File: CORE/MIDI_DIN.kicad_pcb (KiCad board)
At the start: 2 copper layers, 29.5 x 99.8 mm, 60 parts, among them J1 Conn_02x08_Odd_Even, J2 USB_C_Receptacle_USB2.0, J3 Conn_01x04, J5 MAB5100S, J6 MAB5100S, J7 Conn_01x06, Q1 MMBT3906, SW1 SW_SPDT, SW2 SW_Push_DPDT, SW3 PROG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

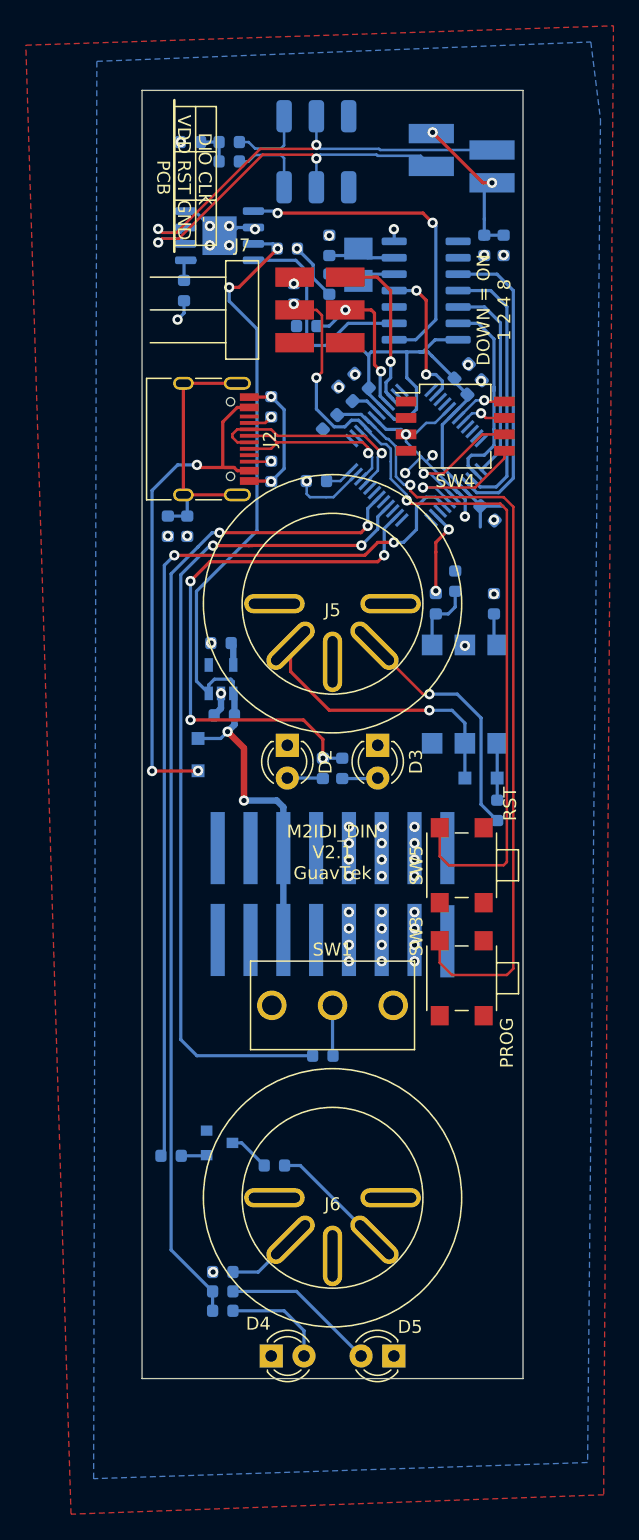
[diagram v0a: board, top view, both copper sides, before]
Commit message: Add 5V power protection
Prevent USB connection from powering other modules
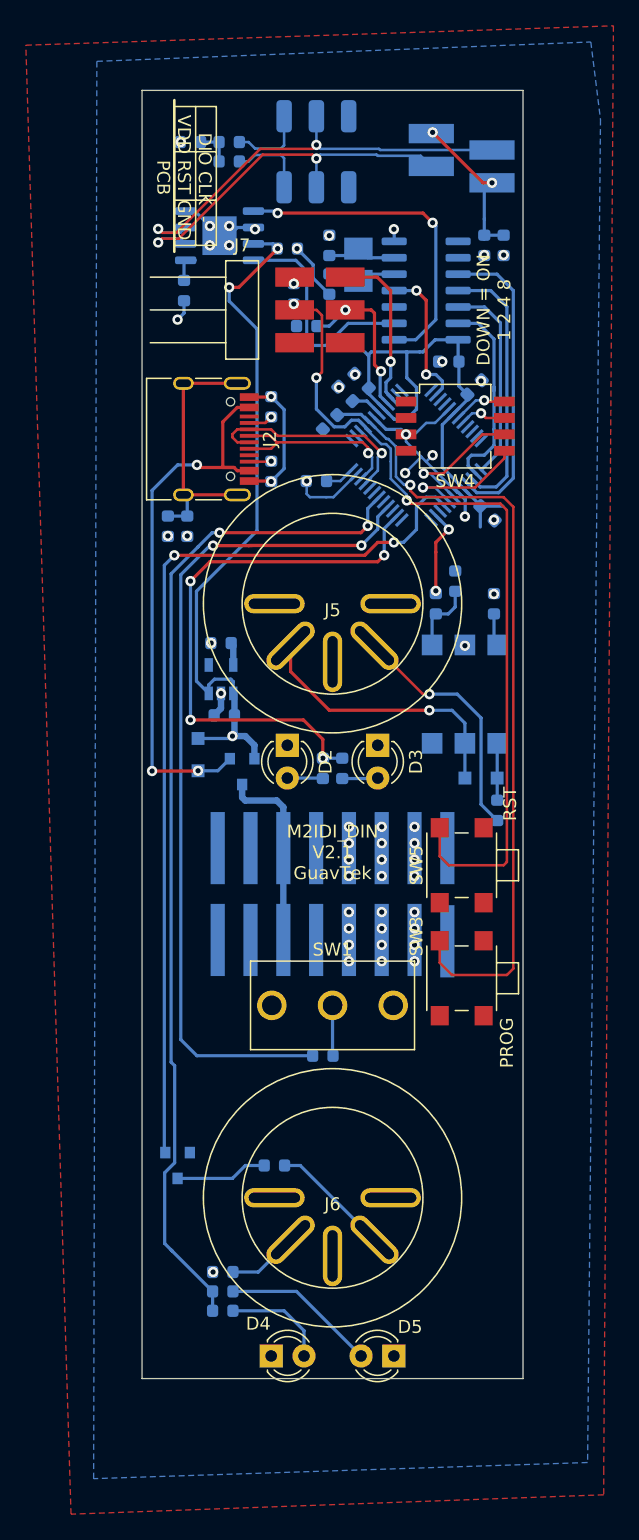
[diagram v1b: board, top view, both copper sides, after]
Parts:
- removed R7: 10k, Resistor_SMD:R_0603_1608Metric
- added Q2: BSS84, Package_TO_SOT_SMD:SOT-23, B.Cu at (78.0, 129.0)
- Q1: value MMBT3906 -> BSS84
- moved Q1 28.8 mm to (83.0, 98.5), turned to 270 degrees
- moved C15 1.25 mm to (99.0, 66.8), turned to 180 degrees
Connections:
- J1 pad 11: +5V -> Net-(J1-Pad11)
- J1 pad 12: +5V -> Net-(J1-Pad11)
- Q1 pad 1: Net-(Q1-Pad1) -> VBUS
- Q1 pad 2: +3V3 -> +5V
- Q1 pad 3: Net-(Q1-Pad3) -> Net-(J1-Pad11)
- R9 pad 1: Net-(Q1-Pad3) -> Net-(Q2-Pad3)
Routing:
- net +5V: track 70.6 -> 54.6 mm, vias 4 -> 3
- net Net-(J1-Pad11): track 0.00 -> 14.8 mm
- net Net-(Q2-Pad3): track 0.00 -> 7.13 mm
- net Net-(Q1-Pad3): track 3.19 -> 0.00 mm
- net VBUS: track 40.7 -> 43.6 mm
- net Net-(Q1-Pad1): track 1.98 -> 0.00 mm
- net ActivityDIN: track 77.7 -> 78.5 mm
- net +3V3: track 48.4 -> 47.7 mm

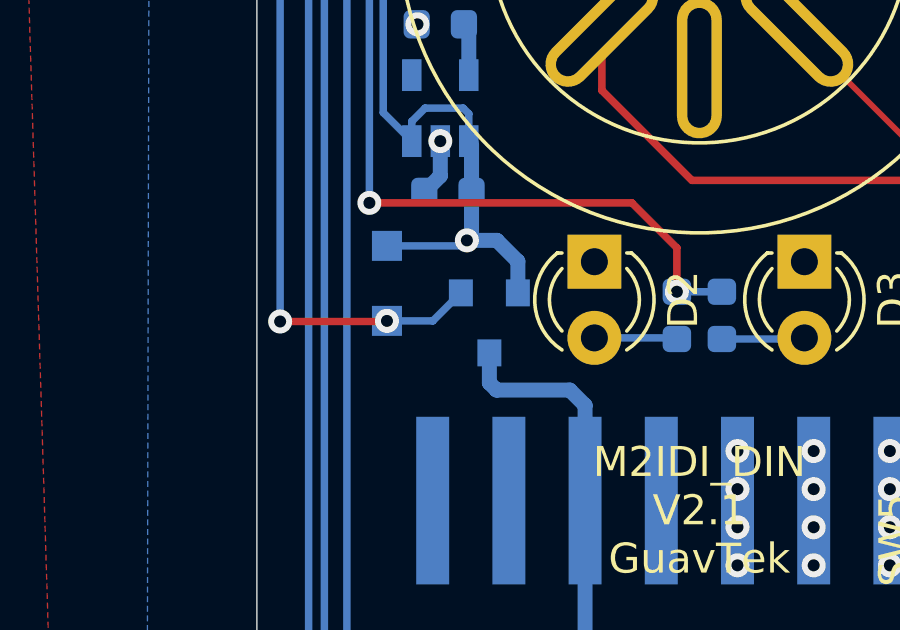
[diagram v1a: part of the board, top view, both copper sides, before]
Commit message: Add pulldown for USB power protection
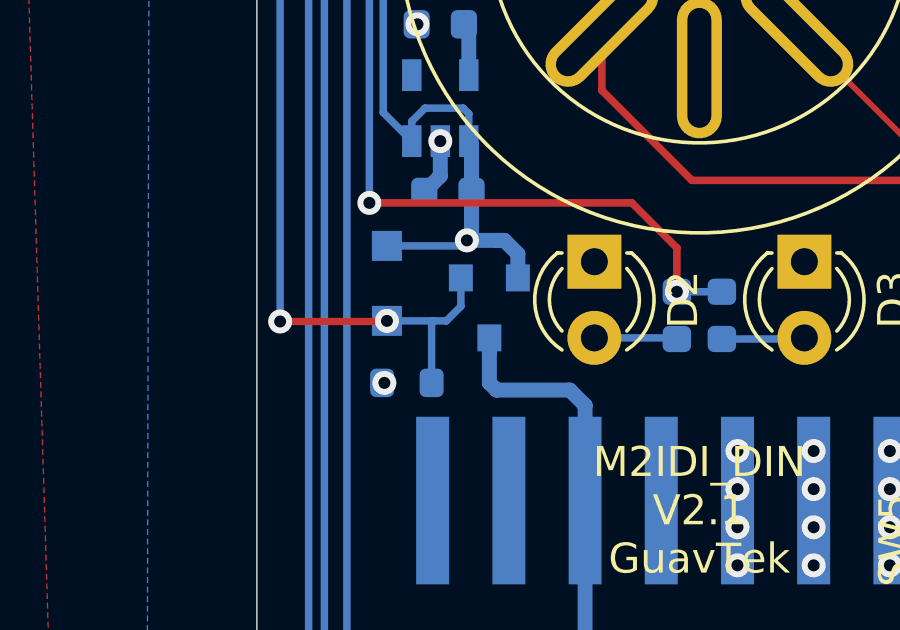
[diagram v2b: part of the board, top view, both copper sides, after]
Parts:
- added R7: 1M, Resistor_SMD:R_0603_1608Metric, B.Cu at (80.2, 100.5)
- moved Q1 0.50 mm to (83.0, 98.0)
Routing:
- net VBUS: track 43.6 -> 46.2 mm
- net Net-(J1-Pad11): track 14.8 -> 15.3 mm
- net GND: vias 55 -> 56

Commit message: Rearrange and re-wire
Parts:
- removed R4: 10k, Resistor_SMD:R_0603_1608Metric
- added Q5: 2N7002, Package_TO_SOT_SMD:SOT-23, B.Cu at (80.5, 134.5)
- added R24: 10k, Resistor_SMD:R_0603_1608Metric, B.Cu at (82.2, 128.0)
- Q2: value BSS84 -> 2N7002
- moved R16 3.07 mm to (99.8, 80.7), turned to 135 degrees
- moved Q2 2.30 mm to (79.5, 130.8)
- moved C4 1.25 mm to (90.0, 76.0), turned to 315 degrees
- moved R8 0.90 mm to (102.2, 100.8), turned to 0 degrees
- moved C2 0.50 mm to (77.8, 79.5)
- moved R1 0.50 mm to (79.2, 79.5)
- moved C3 0.25 mm to (102.8, 85.5)
- moved D6 0.25 mm to (101.8, 99.0)
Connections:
- net MIDIBUS+ renamed M2IDI+
- net MIDIBUS- renamed M2IDI-
- Q2 pad 2: +3V3 -> GND
- R10 pad 2: GND -> Net-(Q5-Pad3)
- R13 pad 2: ActivityBUS -> LED_IN
- R14 pad 2: ActivityDIN -> LED_OUT
- R16 pad 2: Net-(R16-Pad2) -> DIN_IN
- R2 pad 2: ActivityBUS -> LED_IN
- R6 pad 2: ActivityDIN -> LED_OUT
- R9 pad 1: Net-(Q2-Pad3) -> +5V
- U1 pad 26: ActivityBUS -> LED_OUT
- U1 pad 30: ActivityDIN -> LED_IN
- U2 pad 4: Net-(R16-Pad2) -> DIN_IN
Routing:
- net LED_OUT: track 0.00 -> 80.7 mm, vias 0 -> 2
- net ActivityDIN: track 78.5 -> 0.00 mm, vias 2 -> 0
- net +5V: track 54.3 -> 102.8 mm, vias 3 -> 6
- net ActivityBUS: track 43.9 -> 0.00 mm, vias 4 -> 0
- net LED_IN: track 0.00 -> 43.2 mm, vias 0 -> 4
- net DIN_IN: track 6.67 -> 12.4 mm
- net Net-(R16-Pad2): track 5.46 -> 0.00 mm
- net VBUS: track 46.2 -> 41.9 mm, vias 3 -> 1
- net GND: track 48.2 -> 44.4 mm, vias 56 -> 57
- net Net-(J5-Pad4): track 19.0 -> 16.6 mm
- net Net-(Q5-Pad3): track 0.00 -> 1.84 mm
- net +3V3: track 47.7 -> 46.3 mm
- net USB_D+: track 14.9 -> 13.6 mm
- net DIN_OUT: track 70.7 -> 71.9 mm
- net USB_D-: track 17.1 -> 16.0 mm
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
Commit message: Switch to KiCAD 7
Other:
- net class Default removed

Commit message: Fix new DRC
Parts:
- SW1: value SW_SPDT -> SW_Slide_SPDT
- SW2: value SW_Push_DPDT -> SW_Slide_DPDT
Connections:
- J1 pad 1: (no net) -> unconnected-(J1-Pin_1-Pad1)
- J1 pad 10: (no net) -> unconnected-(J1-Pin_10-Pad10)
- J1 pad 13: (no net) -> unconnected-(J1-Pin_13-Pad13)
- J1 pad 14: (no net) -> unconnected-(J1-Pin_14-Pad14)
- J1 pad 15: (no net) -> unconnected-(J1-Pin_15-Pad15)
- J1 pad 16: (no net) -> unconnected-(J1-Pin_16-Pad16)
- J1 pad 2: (no net) -> unconnected-(J1-Pin_2-Pad2)
- J1 pad 9: (no net) -> unconnected-(J1-Pin_9-Pad9)
- J2 pad A8: (no net) -> unconnected-(J2-SBU1-PadA8)
- J2 pad B8: (no net) -> unconnected-(J2-SBU2-PadB8)
- J5 pad 1: (no net) -> unconnected-(J5-Pad1)
- J5 pad 2: (no net) -> unconnected-(J5-Pad2)
- J5 pad 3: (no net) -> unconnected-(J5-Pad3)
- J6 pad 1: (no net) -> unconnected-(J6-Pad1)
- J6 pad 3: (no net) -> unconnected-(J6-Pad3)
- J7 pad 6: (no net) -> unconnected-(J7-Pin_6-Pad6)
- SW2 pad 3: (no net) -> unconnected-(SW2-C-Pad3)
- SW2 pad 6: (no net) -> unconnected-(SW2-C-Pad6)
- U1 pad 1: (no net) -> unconnected-(U1-PA00-Pad1)
- U1 pad 10: (no net) -> unconnected-(U1-PA05-Pad10)
- U1 pad 11: (no net) -> unconnected-(U1-PA06-Pad11)
- U1 pad 12: (no net) -> unconnected-(U1-PA07-Pad12)
- U1 pad 22: (no net) -> unconnected-(U1-PA13-Pad22)
- U1 pad 24: (no net) -> unconnected-(U1-PA15-Pad24)
- U1 pad 25: (no net) -> unconnected-(U1-PA16-Pad25)
- U1 pad 27: (no net) -> unconnected-(U1-PA18-Pad27)
- U1 pad 29: (no net) -> unconnected-(U1-PA20-Pad29)
- U1 pad 3: (no net) -> unconnected-(U1-PA02-Pad3)
- U1 pad 31: (no net) -> unconnected-(U1-PA22-Pad31)
- U1 pad 32: (no net) -> unconnected-(U1-PA23-Pad32)
- U1 pad 37: (no net) -> unconnected-(U1-PB22-Pad37)
- U1 pad 38: (no net) -> unconnected-(U1-PB23-Pad38)
- U1 pad 39: (no net) -> unconnected-(U1-PA27-Pad39)
- U1 pad 4: (no net) -> unconnected-(U1-PA03-Pad4)
- U1 pad 47: (no net) -> unconnected-(U1-PB02-Pad47)
- U1 pad 48: (no net) -> unconnected-(U1-PB03-Pad48)
- U1 pad 9: (no net) -> unconnected-(U1-PA04-Pad9)
- U2 pad 3: (no net) -> unconnected-(U2-Pad3)
- U3 pad 4: (no net) -> unconnected-(U3-NC-Pad4)
- U4 pad 3: (no net) -> unconnected-(U4-CLKO/SOF-Pad3)
- U4 pad 8: (no net) -> unconnected-(U4-~{INT1}/GPIO1-Pad8)
- U4 pad 9: (no net) -> unconnected-(U4-~{INT0}/GPIO0/XSTBY-Pad9)
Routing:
- net VBUS: track 41.9 -> 41.0 mm
